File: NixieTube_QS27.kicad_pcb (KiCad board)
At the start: 2 copper layers, 37 x 56.3 mm, 67 parts, among them J1 Conn_01x06_Male, J2 HV_IN, J3 Conn_01x06_Female, J4 HV_OUT, Q1 MMBTA42LT1, Q10 MMBTA42LT1, Q11 AO3400, Q12 AO3400, Q13 AO3400, Q14 MMBTA42LT1, Q15 MMBTA42LT1, Q2 MMBTA42LT1, Q3 MMBTA42LT1, Q4 MMBTA42LT1, Q5 MMBTA42LT1, Q6 MMBTA42LT1, Q7 MMBTA42LT1, Q8 MMBTA42LT1, Q9 MMBTA42LT1, U1 74HC595D, U2 nixie-tube-qs27, U3 74HC595D, U4 ams1117-5.0

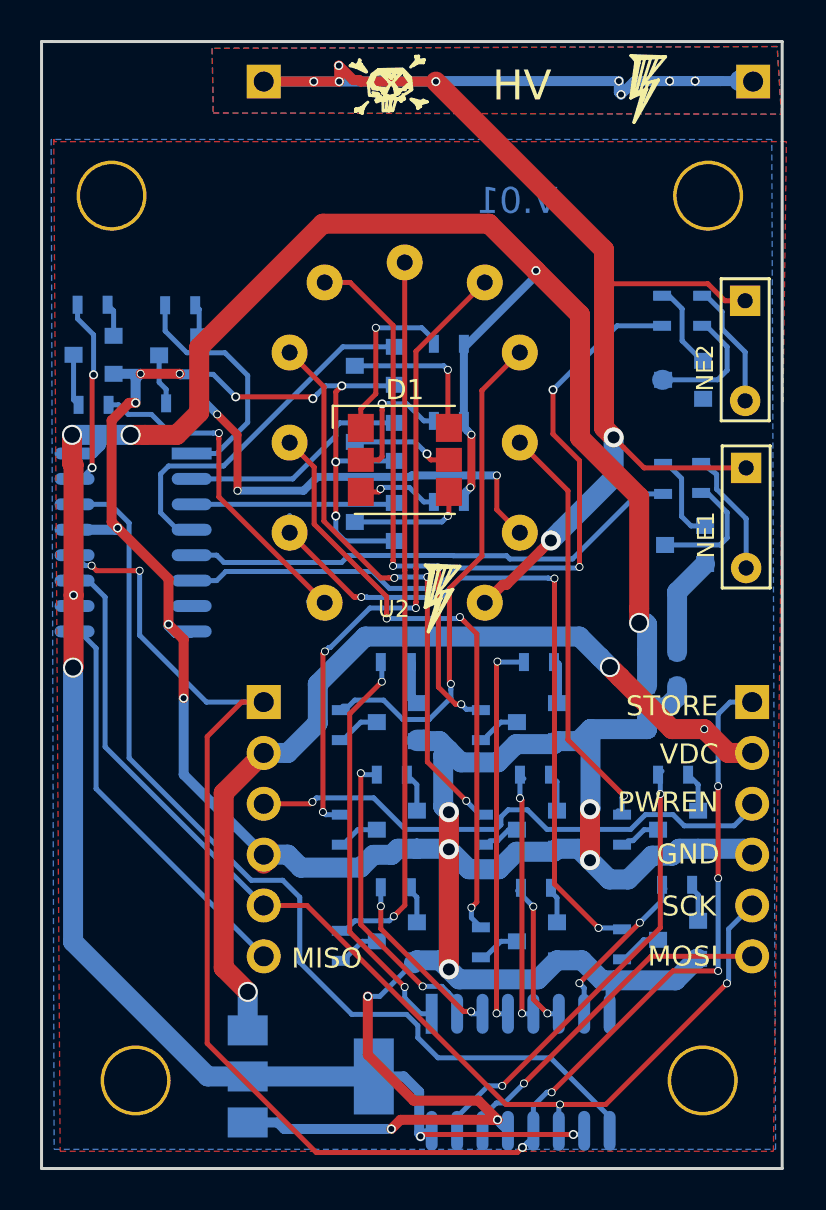
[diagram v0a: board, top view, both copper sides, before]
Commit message: checked all components, adjusted tracks
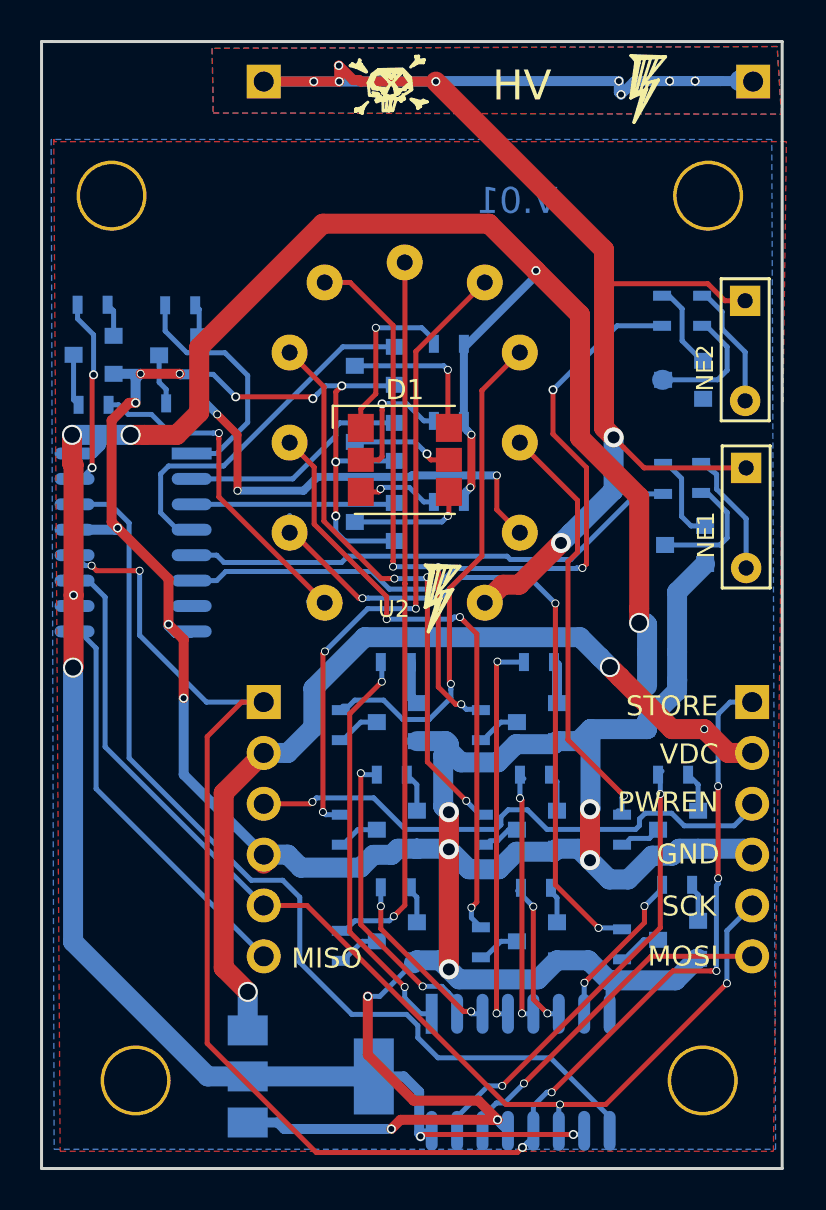
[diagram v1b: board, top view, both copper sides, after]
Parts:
- moved C2 0.26 mm to (182.5, 72.2)
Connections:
- U2 pad 1: Net-(J2-Pad1) -> Net-(R2-Pad1)
- U2 pad 2: Net-(R1-Pad1) -> Net-(R3-Pad1)
- U2 pad 3: Net-(R10-Pad1) -> Net-(R4-Pad1)
- U2 pad 4: Net-(R9-Pad1) -> Net-(R5-Pad1)
- U2 pad 5: Net-(R8-Pad1) -> Net-(R6-Pad1)
- U2 pad 7: Net-(R6-Pad1) -> Net-(R8-Pad1)
- U2 pad 8: Net-(R5-Pad1) -> Net-(R9-Pad1)
- U2 pad 9: Net-(R4-Pad1) -> Net-(R10-Pad1)
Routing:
- net GND: track 180.5 -> 181.6 mm
- net Net-(R3-Pad1): track 35.4 -> 34.8 mm
